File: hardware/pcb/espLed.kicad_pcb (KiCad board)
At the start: 2 copper layers, 23 parts, among them J1 led_strip, J2 flashing, J3 power, Q1 IRF9310TRPBF, Q2 AO3400A, Q3 AO3400A, Q4 AO3400A, SW1 reset, SW2 flash, U1 AMS1117-3.3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

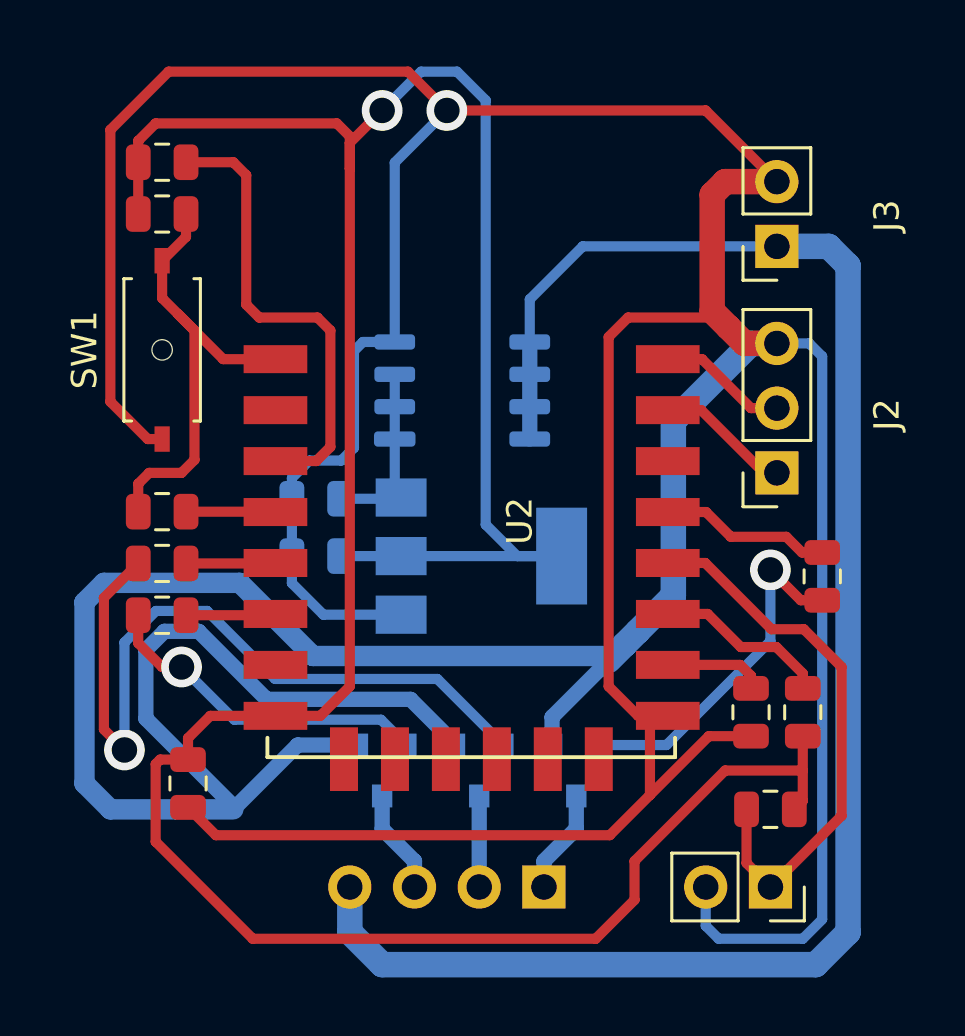
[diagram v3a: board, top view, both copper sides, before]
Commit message: add a board outline and show dimensions
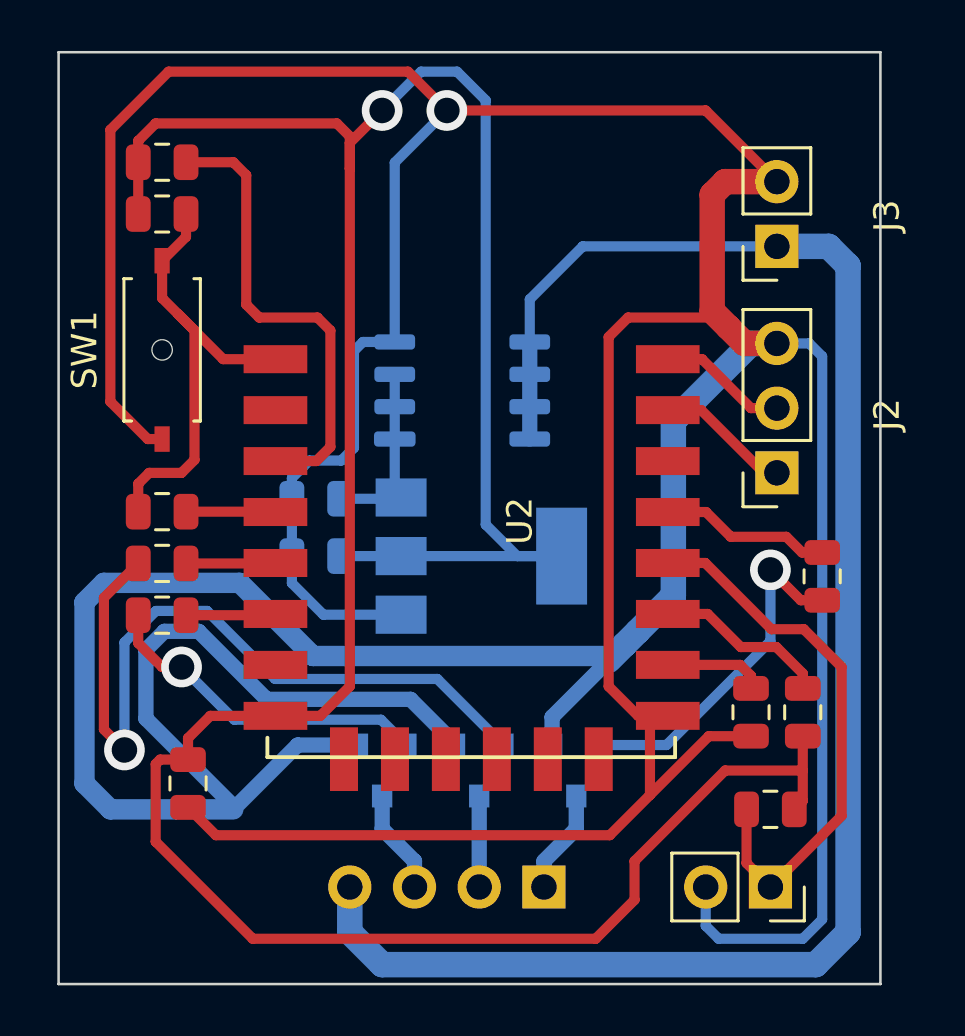
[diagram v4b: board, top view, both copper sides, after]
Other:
- board outline added: 32.3 x 36.6 mm
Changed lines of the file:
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@@
   (general
     (thickness 1.6)
-    (drawings 0)
+    (drawings 6)
     (tracks 221)
     (zones 0)
@@
     )
   )
+  (dimension 36.576 (width 0.15) (layer Dwgs.User)
+    (gr_text "36,576 mm" (at 199.674 124.46 270) (layer Dwgs.User)
+      (effects (font (size 1 1) (thickness 0.15)))
+    )
+    (feature1 (pts (xy 195.326 142.748) (xy 198.960421 142.748)))
+    (feature2 (pts (xy 195.326 106.172) (xy 198.960421 106.172)))
+    (crossbar (pts (xy 198.374 106.172) (xy 198.374 142.748)))
+    (arrow1a (pts (xy 198.374 142.748) (xy 197.787579 141.621496)))
+    (arrow1b (pts (xy 198.374 142.748) (xy 198.960421 141.621496)))
+    (arrow2a (pts (xy 198.374 106.172) (xy 197.787579 107.298504)))
+    (arrow2b (pts (xy 198.374 106.172) (xy 198.960421 107.298504)))
+  )
+  (dimension 32.258 (width 0.15) (layer Dwgs.User)
+    (gr_text "32,258 mm" (at 179.197 102.586) (layer Dwgs.User)
+      (effects (font (size 1 1) (thickness 0.15)))
+    )
+    (feature1 (pts (xy 195.326 106.172) (xy 195.326 103.299579)))
+    (feature2 (pts (xy 163.068 106.172) (xy 163.068 103.299579)))
+    (crossbar (pts (xy 163.068 103.886) (xy 195.326 103.886)))
+    (arrow1a (pts (xy 195.326 103.886) (xy 194.199496 104.472421)))
+    (arrow1b (pts (xy 195.326 103.886) (xy 194.199496 103.299579)))
+    (arrow2a (pts (xy 163.068 103.886) (xy 164.194504 104.472421)))
+    (arrow2b (pts (xy 163.068 103.886) (xy 164.194504 103.299579)))
+  )
+  (gr_line (start 195.326 106.172) (end 195.326 142.748) (layer Edge.Cuts) (width 0.1))
+  (gr_line (start 163.068 106.172) (end 195.326 106.172) (layer Edge.Cuts) (width 0.1))
+  (gr_line (start 163.068 142.748) (end 163.068 106.172) (layer Edge.Cuts) (width 0.1))
+  (gr_line (start 195.326 142.748) (end 163.068 142.748) (layer Edge.Cuts) (width 0.1))
   (segment (start 172.2245 127.0125) (end 172.2245 125.95) (width 0.4) (layer B.Cu) (net 1))
   (segment (start 173.462 128.25) (end 172.2245 127.0125) (width 0.4) (layer B.Cu) (net 1))

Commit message: move power circuitry upwards and make traces power nearby thicker
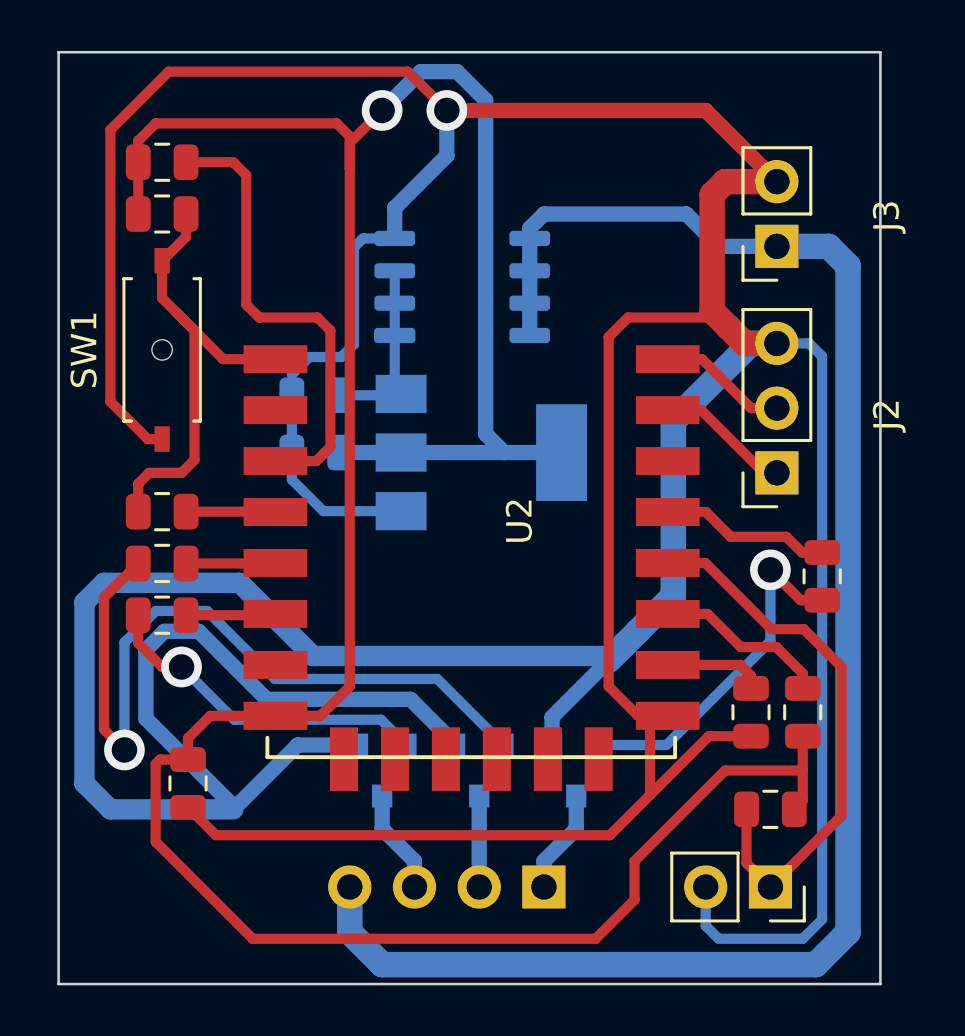
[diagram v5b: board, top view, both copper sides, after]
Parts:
- moved C1 4.06 mm to (173.2, 119.6)
- moved C2 4.06 mm to (173.2, 121.9)
- moved Q1 4.06 mm to (178.9, 115.4)
- moved U1 4.06 mm to (179.7, 121.9)
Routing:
- net +3V3: track 116.7 -> 110.7 mm
- net GND: track 246.0 -> 241.2 mm
- net /12v_in: track 67.7 -> 66.3 mm

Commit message: make power connections to ESP thicker
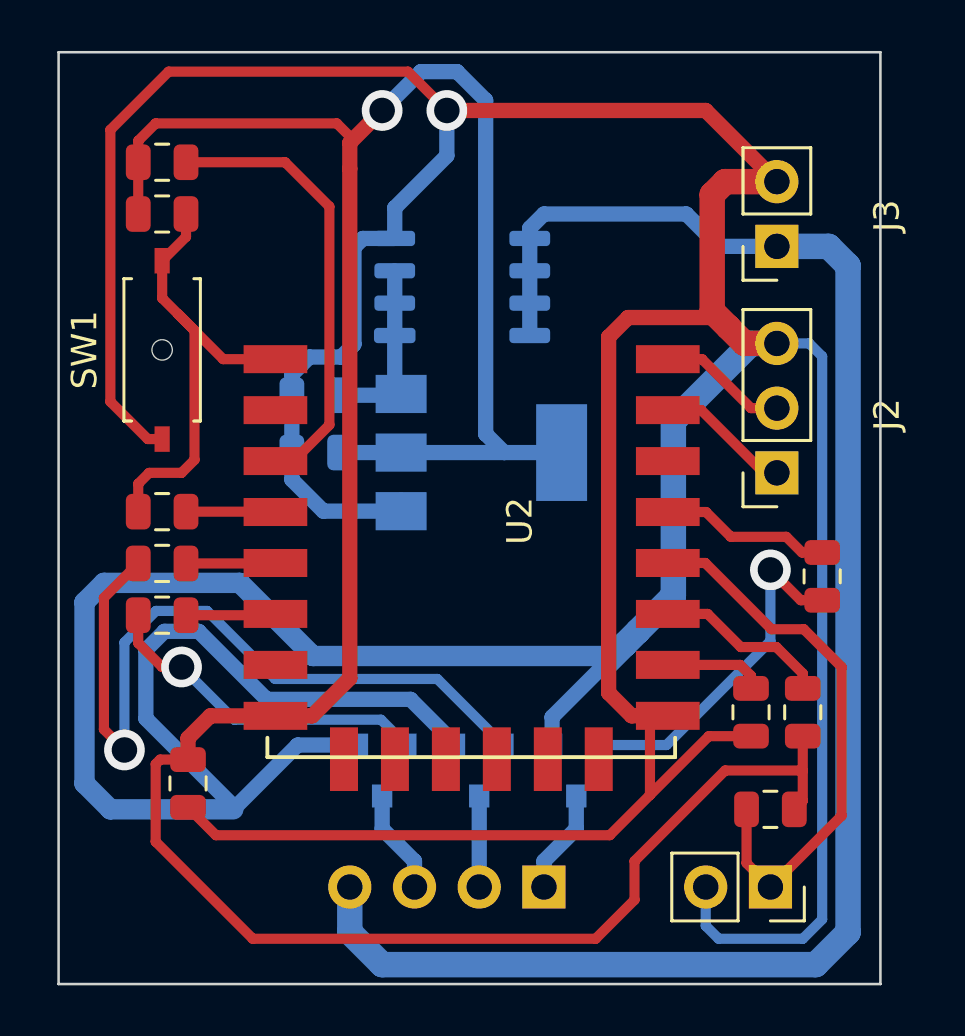
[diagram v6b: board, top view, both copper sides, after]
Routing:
- net GND: track 241.2 -> 242.2 mm
- net Net-(R6-Pad2): track 17.7 -> 17.0 mm

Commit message: disconnect GND of two transistors, move decoupling capacitor to bottom
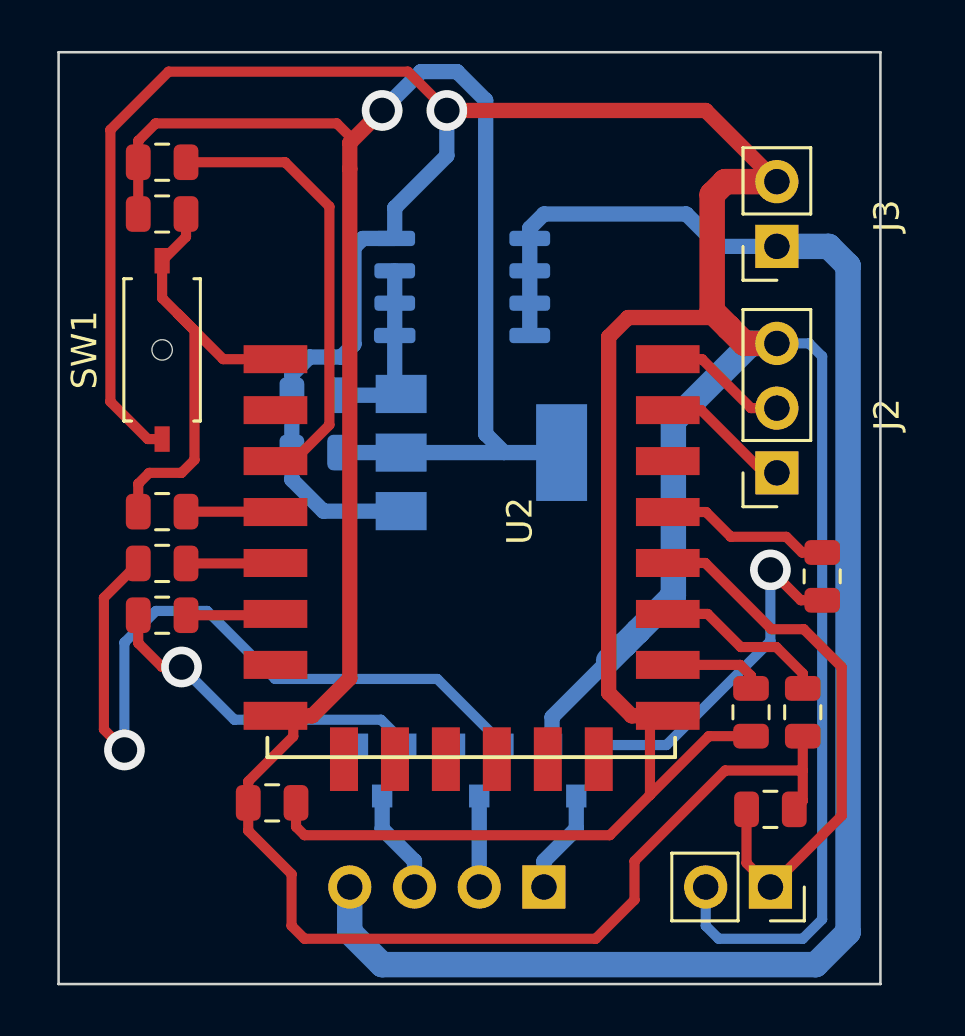
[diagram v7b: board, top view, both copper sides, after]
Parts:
- moved C3 3.39 mm to (171.4, 135.6), turned to 0 degrees
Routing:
- net GND: track 242.2 -> 175.1 mm
- net +3V3: track 110.5 -> 103.8 mm
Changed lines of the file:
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@@
     (thickness 1.6)
     (drawings 6)
-    (tracks 218)
+    (tracks 202)
     (zones 0)
     (modules 23)
@@
   )
   (setup
-    (last_trace_width 0.6)
+    (last_trace_width 0.4)
     (user_trace_width 0.4)
     (user_trace_width 0.6)
@@
   )
   (module Capacitor_SMD:C_0805_2012Metric (layer F.Cu)
-    (at 168.148 134.874 270)
+    (at 171.45 135.636)
     (descr "Capacitor SMD 0805 (2012 Metric), square (rectangular) end terminal, IPC_7351 nominal, (Body size source: https://docs.google.com/spreadsheets/d/1BsfQQcO9C6DZCsRaXUlFlo91Tg2WpOkGARC1WS5S8t0/edit?usp=sharing), generated with kicad-footprint-generator")
     (tags capacitor)
     (attr smd)
-    (fp_text reference C3 (at 0 -1.65 90) (layer F.SilkS) hide
-      (effects (font (size 1 1) (thickness 0.15)))
-    )
-    (fp_text value 100uF (at 0 1.65 90) (layer F.Fab) hide
+    (fp_text reference C3 (at 0 -1.65) (layer F.SilkS) hide
+      (effects (font (size 1 1) (thickness 0.15)))
+    )
+    (fp_text value 100uF (at 0 1.65) (layer F.Fab) hide
       (effects (font (size 1 1) (thickness 0.15)))
     )
@@
     (fp_line (start 1.68 -0.95) (end 1.68 0.95) (layer F.CrtYd) (width 0.05))
     (fp_line (start 1.68 0.95) (end -1.68 0.95) (layer F.CrtYd) (width 0.05))
-    (fp_text user %R (at 0 0 90) (layer F.Fab) hide
+    (fp_text user %R (at 0 0) (layer F.Fab) hide
       (effects (font (size 0.5 0.5) (thickness 0.08)))
     )
-    (pad 2 smd roundrect (at 0.9375 0 270) (size 0.975 1.4) (layers F.Cu F.Paste F.Mask) (roundrect_rratio 0.25)
-      (net 1 GND))
-    (pad 1 smd roundrect (at -0.9375 0 270) (size 0.975 1.4) (layers F.Cu F.Paste F.Mask) (roundrect_rratio 0.25)
+    (pad 2 smd roundrect (at 0.9375 0) (size 0.975 1.4) (layers F.Cu F.Paste F.Mask) (roundrect_rratio 0.25)
+      (net 1 GND))
+    (pad 1 smd roundrect (at -0.9375 0) (size 0.975 1.4) (layers F.Cu F.Paste F.Mask) (roundrect_rratio 0.25)
       (net 3 +3V3))
     (model ${KISYS3DMOD}/Capacitor_SMD.3dshapes/C_0805_2012Metric.wrl
@@
   (segment (start 188.590501 133.0175) (end 186.28 135.328001) (width 0.4) (layer F.Cu) (net 1))
   (segment (start 190.246 133.0175) (end 188.590501 133.0175) (width 0.4) (layer F.Cu) (net 1))
-  (segment (start 184.702001 136.906) (end 169.2425 136.906) (width 0.4) (layer F.Cu) (net 1))
-  (segment (start 169.2425 136.906) (end 168.148 135.8115) (width 0.4) (layer F.Cu) (net 1))
-  (segment (start 186.28 135.328001) (end 184.702001 136.906) (width 0.4) (layer F.Cu) (net 1))
   (segment (start 192.532 117.602) (end 191.262 117.602) (width 0.4) (layer B.Cu) (net 1))
   (segment (start 193.04 118.11) (end 192.532 117.602) (width 0.4) (layer B.Cu) (net 1))
@@
   (segment (start 182.438 132.268) (end 185.293 129.413) (width 0.6) (layer B.Cu) (net 1))
   (segment (start 184.658 130.048) (end 185.293 129.413) (width 1) (layer B.Cu) (net 1))
-  (segment (start 172.45 133.366) (end 169.926 135.89) (width 0.6) (layer B.Cu) (net 1))
-  (segment (start 174.818 133.366) (end 172.45 133.366) (width 0.6) (layer B.Cu) (net 1))
   (segment (start 184.912 129.794) (end 185.293 129.413) (width 0.4) (layer B.Cu) (net 1))
   (segment (start 185.801 128.905) (end 187.198 127.508) (width 1) (layer B.Cu) (net 1))
   (segment (start 185.293 129.413) (end 185.801 128.905) (width 1) (layer B.Cu) (net 1))
-  (segment (start 169.926 135.760662) (end 169.926 135.89) (width 0.6) (layer B.Cu) (net 1))
-  (segment (start 166.493999 132.328661) (end 169.926 135.760662) (width 0.6) (layer B.Cu) (net 1))
   (segment (start 178.628 133.366) (end 178.628 133.316) (width 0.6) (layer B.Cu) (net 1))
-  (segment (start 166.493999 129.629999) (end 166.493999 132.328661) (width 0.6) (layer B.Cu) (net 1))
-  (segment (start 171.236002 131.572) (end 168.566001 128.901999) (width 0.6) (layer B.Cu) (net 1))
-  (segment (start 178.628 133.316) (end 176.884 131.572) (width 0.6) (layer B.Cu) (net 1))
-  (segment (start 168.566001 128.901999) (end 167.221999 128.901999) (width 0.6) (layer B.Cu) (net 1))
-  (segment (start 167.221999 128.901999) (end 166.493999 129.629999) (width 0.6) (layer B.Cu) (net 1))
-  (segment (start 176.884 131.572) (end 171.236002 131.572) (width 0.6) (layer B.Cu) (net 1))
-  (segment (start 173.05198 129.87198) (end 184.83402 129.87198) (width 0.8) (layer B.Cu) (net 1))
-  (segment (start 170.18 127) (end 173.05198 129.87198) (width 0.8) (layer B.Cu) (net 1))
-  (segment (start 164.846 127) (end 170.18 127) (width 0.8) (layer B.Cu) (net 1))
-  (segment (start 164.084 127.762) (end 164.846 127) (width 0.8) (layer B.Cu) (net 1))
-  (segment (start 164.084 134.874) (end 164.084 127.762) (width 0.8) (layer B.Cu) (net 1))
   (segment (start 184.83402 129.87198) (end 185.801 128.905) (width 0.8) (layer B.Cu) (net 1))
-  (segment (start 165.1 135.89) (end 164.084 134.874) (width 0.8) (layer B.Cu) (net 1))
-  (segment (start 169.926 135.89) (end 165.1 135.89) (width 0.8) (layer B.Cu) (net 1))
   (segment (start 189.23 111.252) (end 191.262 111.252) (width 1) (layer F.Cu) (net 1))
   (segment (start 188.722 111.76) (end 189.23 111.252) (width 1) (layer F.Cu) (net 1))
@@
   (segment (start 184.658 131.318) (end 184.658 117.348) (width 0.6) (layer F.Cu) (net 1))
   (segment (start 186.28 132.22) (end 185.56 132.22) (width 0.6) (layer F.Cu) (net 1))
+  (segment (start 172.3875 136.5735) (end 172.3875 135.636) (width 0.4) (layer F.Cu) (net 1))
+  (segment (start 172.72 136.906) (end 172.3875 136.5735) (width 0.4) (layer F.Cu) (net 1))
+  (segment (start 184.702001 136.906) (end 172.72 136.906) (width 0.4) (layer F.Cu) (net 1))
+  (segment (start 186.28 135.328001) (end 184.702001 136.906) (width 0.4) (layer F.Cu) (net 1))
   (segment (start 174.0995 119.636) (end 176.462 119.636) (width 0.6) (layer B.Cu) (net 2))
   (segment (start 176.262 117.291) (end 176.262 114.751) (width 0.6) (layer B.Cu) (net 2))
@@
   (segment (start 192.278 133.0175) (end 192.278 134.366) (width 0.4) (layer F.Cu) (net 3))
   (segment (start 192.278 134.366) (end 192.278 135.5575) (width 0.4) (layer F.Cu) (net 3))
-  (segment (start 168.148 133.096) (end 168.148 133.9365) (width 0.6) (layer F.Cu) (net 3))
-  (segment (start 169.024 132.22) (end 168.148 133.096) (width 0.6) (layer F.Cu) (net 3))
-  (segment (start 172.28 132.22) (end 169.024 132.22) (width 0.6) (layer F.Cu) (net 3))
-  (segment (start 167.0535 133.9365) (end 168.148 133.9365) (width 0.4) (layer F.Cu) (net 3))
-  (segment (start 170.688 140.97) (end 166.878 137.16) (width 0.4) (layer F.Cu) (net 3))
-  (segment (start 184.15 140.97) (end 170.688 140.97) (width 0.4) (layer F.Cu) (net 3))
-  (segment (start 185.674 139.446) (end 184.15 140.97) (width 0.4) (layer F.Cu) (net 3))
-  (segment (start 185.674 137.922) (end 185.674 139.446) (width 0.4) (layer F.Cu) (net 3))
-  (segment (start 189.23 134.366) (end 185.674 137.922) (width 0.4) (layer F.Cu) (net 3))
-  (segment (start 192.278 134.366) (end 189.23 134.366) (width 0.4) (layer F.Cu) (net 3))
   (segment (start 166.1945 110.49) (end 166.1945 109.9035) (width 0.4) (layer F.Cu) (net 3))
-  (segment (start 166.878 137.16) (end 166.878 134.112) (width 0.4) (layer F.Cu) (net 3))
-  (segment (start 166.878 134.112) (end 167.0535 133.9365) (width 0.4) (layer F.Cu) (net 3))
   (segment (start 173.99 108.966) (end 174.498 109.474) (width 0.4) (layer F.Cu) (net 3))
   (segment (start 166.878 108.966) (end 173.99 108.966) (width 0.4) (layer F.Cu) (net 3))
@@
   (segment (start 174.498 130.7465) (end 173.0245 132.22) (width 0.6) (layer F.Cu) (net 3))
   (segment (start 174.498 110.744) (end 174.498 130.7465) (width 0.6) (layer F.Cu) (net 3))
+  (segment (start 172.28 133.028) (end 172.28 132.22) (width 0.4) (layer F.Cu) (net 3))
+  (segment (start 170.5125 134.7955) (end 172.28 133.028) (width 0.4) (layer F.Cu) (net 3))
+  (segment (start 170.5125 135.636) (end 170.5125 134.7955) (width 0.4) (layer F.Cu) (net 3))
+  (segment (start 172.212 140.462) (end 172.212 138.43) (width 0.4) (layer F.Cu) (net 3))
+  (segment (start 170.5125 136.7305) (end 170.5125 135.636) (width 0.4) (layer F.Cu) (net 3))
+  (segment (start 172.212 138.43) (end 170.5125 136.7305) (width 0.4) (layer F.Cu) (net 3))
+  (segment (start 172.72 140.97) (end 172.212 140.462) (width 0.4) (layer F.Cu) (net 3))
+  (segment (start 184.15 140.97) (end 172.72 140.97) (width 0.4) (layer F.Cu) (net 3))
+  (segment (start 185.674 139.446) (end 184.15 140.97) (width 0.4) (layer F.Cu) (net 3))
+  (segment (start 185.674 137.922) (end 185.674 139.446) (width 0.4) (layer F.Cu) (net 3))
+  (segment (start 189.23 134.366) (end 185.674 137.922) (width 0.4) (layer F.Cu) (net 3))
+  (segment (start 192.278 134.366) (end 189.23 134.366) (width 0.4) (layer F.Cu) (net 3))
   (segment (start 175.768 136.652) (end 177.038 137.922) (width 0.6) (layer B.Cu) (net 4))
   (segment (start 177.038 137.922) (end 177.038 138.938) (width 0.6) (layer B.Cu) (net 4))
